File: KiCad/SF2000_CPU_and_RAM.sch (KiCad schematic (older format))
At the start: 5 parts, among them U10 IS61WV20488FBLL-10TLI, U11 IS61WV20488FBLL-10TLI, U12 IS61WV20488FBLL-10TLI, U8 68000D, U9 IS61WV20488FBLL-10TLI

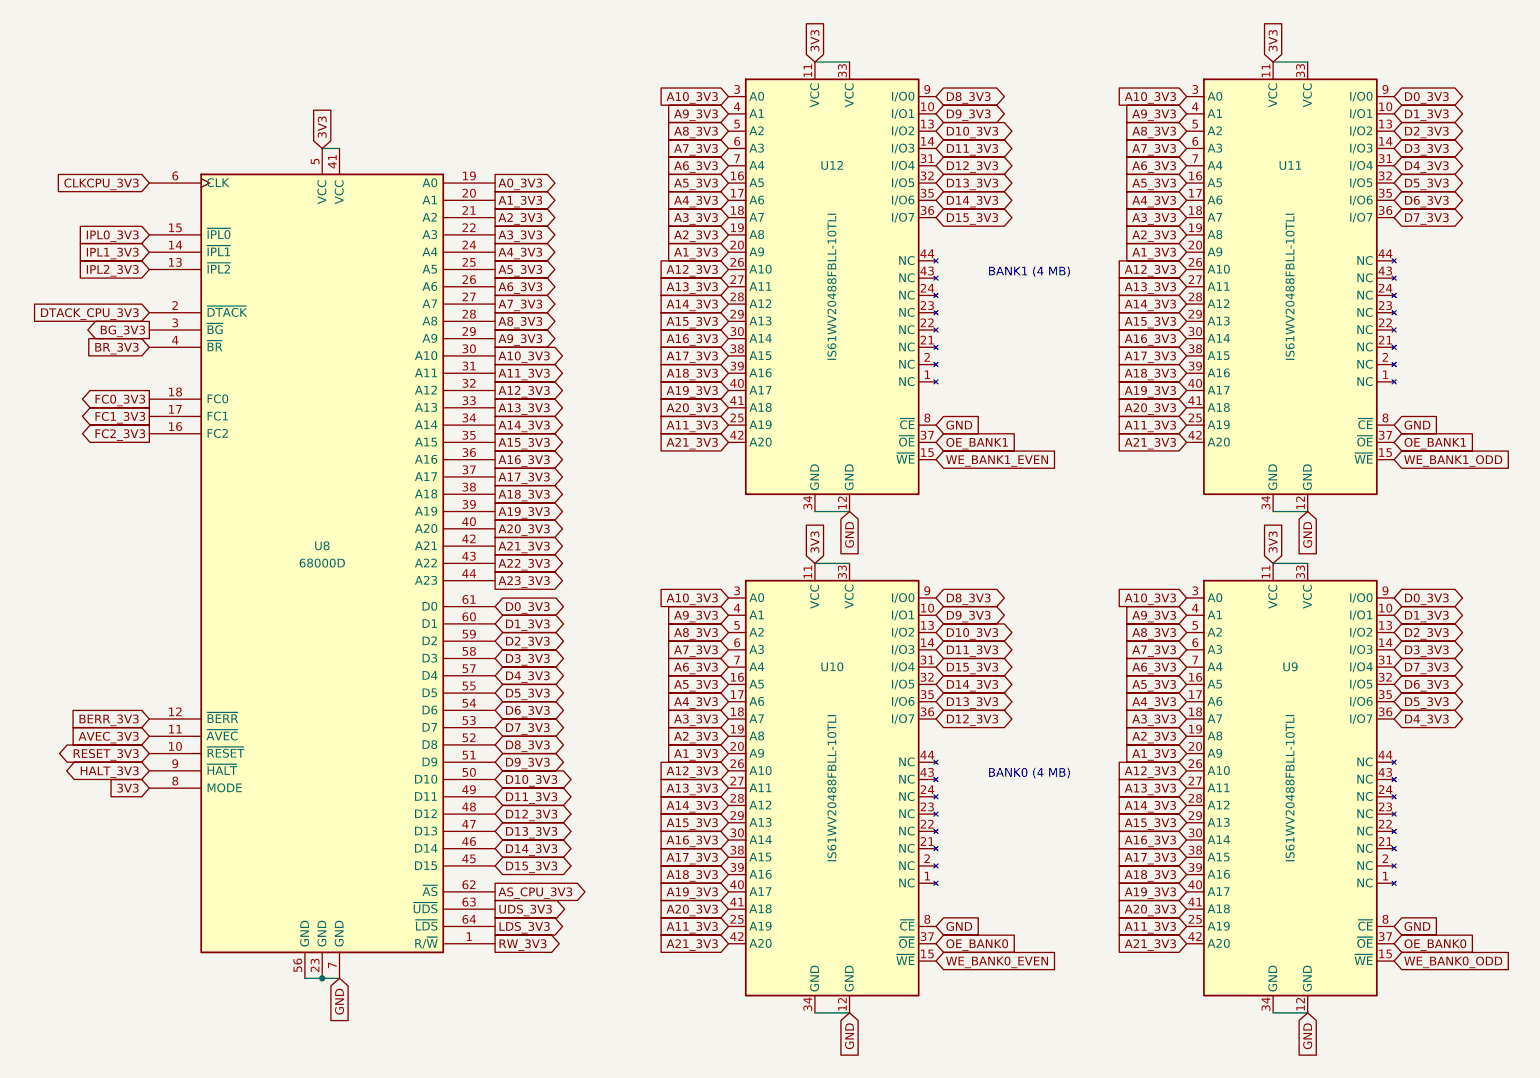
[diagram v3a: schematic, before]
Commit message: reconnected SRAMs and rerouted, and added a lot of caps
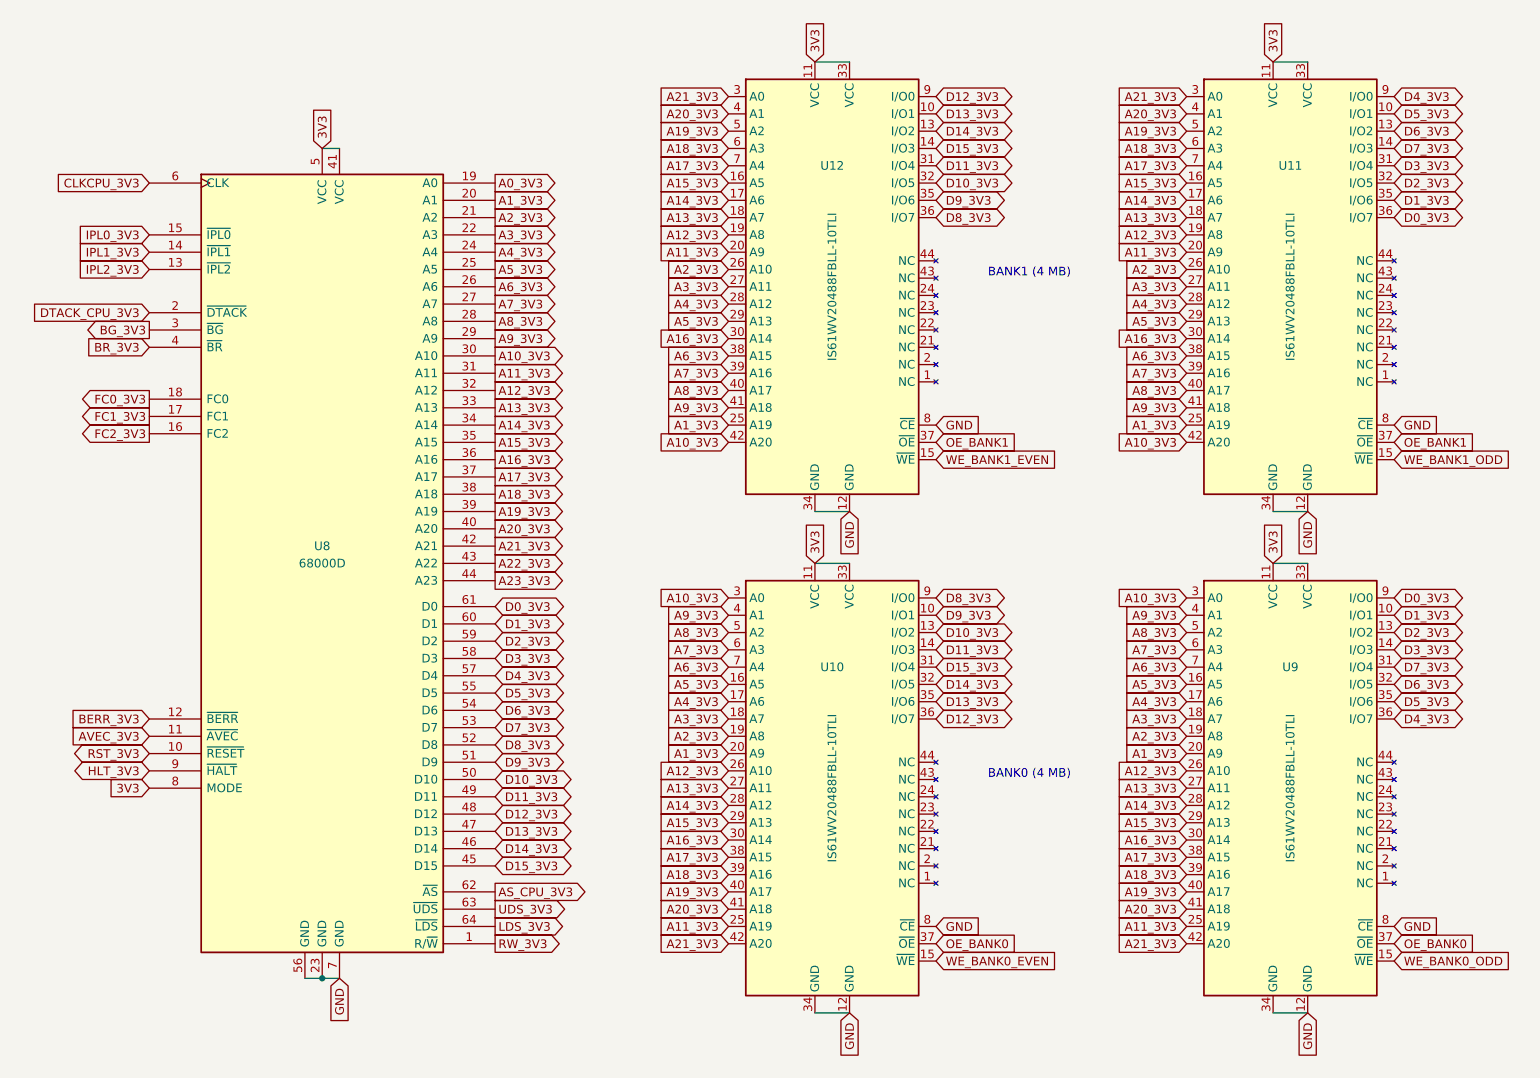
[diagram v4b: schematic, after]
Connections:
- net A10_3V3: now also U11.42 (A20), U12.42 (A20); no longer U11.3 (A0), U12.3 (A0)
- net A11_3V3: now also U11.20 (A9), U12.20 (A9); no longer U11.25 (A19), U12.25 (A19)
- net A12_3V3: now also U11.19 (A8), U12.19 (A8); no longer U11.26 (A10), U12.26 (A10)
- net A13_3V3: now also U11.18 (A7), U12.18 (A7); no longer U11.27 (A11), U12.27 (A11)
- net A14_3V3: now also U11.17 (A6), U12.17 (A6); no longer U11.28 (A12), U12.28 (A12)
- net A15_3V3: now also U11.16 (A5), U12.16 (A5); no longer U11.29 (A13), U12.29 (A13)
- net A17_3V3: now also U11.7 (A4), U12.7 (A4); no longer U11.38 (A15), U12.38 (A15)
- net A18_3V3: now also U11.6 (A3), U12.6 (A3); no longer U11.39 (A16), U12.39 (A16)
- net A19_3V3: now also U11.5 (A2), U12.5 (A2); no longer U11.40 (A17), U12.40 (A17)
- net A1_3V3: now also U11.25 (A19), U12.25 (A19); no longer U11.20 (A9), U12.20 (A9)
- net A20_3V3: now also U11.4 (A1), U12.4 (A1); no longer U11.41 (A18), U12.41 (A18)
- net A21_3V3: now also U11.3 (A0), U12.3 (A0); no longer U11.42 (A20), U12.42 (A20)
- net A2_3V3: now also U11.26 (A10), U12.26 (A10); no longer U11.19 (A8), U12.19 (A8)
- net A3_3V3: now also U11.27 (A11), U12.27 (A11); no longer U11.18 (A7), U12.18 (A7)
- net A4_3V3: now also U11.28 (A12), U12.28 (A12); no longer U11.17 (A6), U12.17 (A6)
- net A5_3V3: now also U11.29 (A13), U12.29 (A13); no longer U11.16 (A5), U12.16 (A5)
- net A6_3V3: now also U11.38 (A15), U12.38 (A15); no longer U11.7 (A4), U12.7 (A4)
- net A7_3V3: now also U11.39 (A16), U12.39 (A16); no longer U11.6 (A3), U12.6 (A3)
- net A8_3V3: now also U11.40 (A17), U12.40 (A17); no longer U11.5 (A2), U12.5 (A2)
- net A9_3V3: now also U11.41 (A18), U12.41 (A18); no longer U11.4 (A1), U12.4 (A1)
- net D0_3V3: now also U11.36 (I/O7); no longer U11.9 (I/O0)
- net D10_3V3: now also U12.32 (I/O5); no longer U12.13 (I/O2)
- net D11_3V3: now also U12.31 (I/O4); no longer U12.14 (I/O3)
- net D12_3V3: now also U12.9 (I/O0); no longer U12.31 (I/O4)
- net D13_3V3: now also U12.10 (I/O1); no longer U12.32 (I/O5)
- net D14_3V3: now also U12.13 (I/O2); no longer U12.35 (I/O6)
- net D15_3V3: now also U12.14 (I/O3); no longer U12.36 (I/O7)
- net D1_3V3: now also U11.35 (I/O6); no longer U11.10 (I/O1)
- net D2_3V3: now also U11.32 (I/O5); no longer U11.13 (I/O2)
- net D3_3V3: now also U11.31 (I/O4); no longer U11.14 (I/O3)
- net D4_3V3: now also U11.9 (I/O0); no longer U11.31 (I/O4)
- net D5_3V3: now also U11.10 (I/O1); no longer U11.32 (I/O5)
- net D6_3V3: now also U11.13 (I/O2); no longer U11.35 (I/O6)
- net D7_3V3: now also U11.14 (I/O3); no longer U11.36 (I/O7)
- net D8_3V3: now also U12.36 (I/O7); no longer U12.9 (I/O0)
- net D9_3V3: now also U12.35 (I/O6); no longer U12.10 (I/O1)
- net HALT_3V3 renamed HLT_3V3
- net RESET_3V3 renamed RST_3V3
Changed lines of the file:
@@
 AVEC_3V3
 Text GLabel 1500 4800 0    50   BiDi ~ 0
-RESET_3V3
+RST_3V3
 Text GLabel 1500 4900 0    50   BiDi ~ 0
-HALT_3V3
+HLT_3V3
 Text GLabel 1500 2450 0    50   Input ~ 0
 BR_3V3
@@
 Wire Wire Line
 	5350 6300 5550 6300
+Text GLabel 8700 1700 2    50   BiDi ~ 0
+D0_3V3
+Text GLabel 8700 1600 2    50   BiDi ~ 0
+D1_3V3
+Text GLabel 8700 1500 2    50   BiDi ~ 0
+D2_3V3
+Text GLabel 8700 1400 2    50   BiDi ~ 0
+D3_3V3
 Text GLabel 8700 1000 2    50   BiDi ~ 0
-D0_3V3
+D4_3V3
 Text GLabel 8700 1100 2    50   BiDi ~ 0
-D1_3V3
+D5_3V3
 Text GLabel 8700 1200 2    50   BiDi ~ 0
-D2_3V3
+D6_3V3
 Text GLabel 8700 1300 2    50   BiDi ~ 0
-D3_3V3
-Text GLabel 8700 1400 2    50   BiDi ~ 0
-D4_3V3
-Text GLabel 8700 1500 2    50   BiDi ~ 0
-D5_3V3
-Text GLabel 8700 1600 2    50   BiDi ~ 0
-D6_3V3
-Text GLabel 8700 1700 2    50   BiDi ~ 0
 D7_3V3
 Text GLabel 8700 3900 2    50   BiDi ~ 0
@@
 Text GLabel 6050 4300 2    50   BiDi ~ 0
 D15_3V3
+Text GLabel 6050 1700 2    50   BiDi ~ 0
+D8_3V3
+Text GLabel 6050 1600 2    50   BiDi ~ 0
+D9_3V3
+Text GLabel 6050 1500 2    50   BiDi ~ 0
+D10_3V3
+Text GLabel 6050 1400 2    50   BiDi ~ 0
+D11_3V3
 Text GLabel 6050 1000 2    50   BiDi ~ 0
-D8_3V3
+D12_3V3
 Text GLabel 6050 1100 2    50   BiDi ~ 0
-D9_3V3
+D13_3V3
 Text GLabel 6050 1200 2    50   BiDi ~ 0
-D10_3V3
+D14_3V3
 Text GLabel 6050 1300 2    50   BiDi ~ 0
-D11_3V3
-Text GLabel 6050 1400 2    50   BiDi ~ 0
-D12_3V3
-Text GLabel 6050 1500 2    50   BiDi ~ 0
-D13_3V3
-Text GLabel 6050 1600 2    50   BiDi ~ 0
-D14_3V3
-Text GLabel 6050 1700 2    50   BiDi ~ 0
 D15_3V3
+Text GLabel 4850 2900 0    50   Input ~ 0
+A1_3V3
+Text GLabel 4850 2000 0    50   Input ~ 0
+A2_3V3
+Text GLabel 4850 2100 0    50   Input ~ 0
+A3_3V3
+Text GLabel 4850 2200 0    50   Input ~ 0
+A4_3V3
+Text GLabel 4850 2300 0    50   Input ~ 0
+A5_3V3
+Text GLabel 4850 2500 0    50   Input ~ 0
+A6_3V3
+Text GLabel 4850 2600 0    50   Input ~ 0
+A7_3V3
+Text GLabel 4850 2700 0    50   Input ~ 0
+A8_3V3
+Text GLabel 4850 2800 0    50   Input ~ 0
+A9_3V3
+Text GLabel 4850 3000 0    50   Input ~ 0
+A10_3V3
 Text GLabel 4850 1900 0    50   Input ~ 0
-A1_3V3
+A11_3V3
 Text GLabel 4850 1800 0    50   Input ~ 0
-A2_3V3
+A12_3V3
 Text GLabel 4850 1700 0    50   Input ~ 0
-A3_3V3
+A13_3V3
 Text GLabel 4850 1600 0    50   Input ~ 0
-A4_3V3
+A14_3V3
 Text GLabel 4850 1500 0    50   Input ~ 0
-A5_3V3
-Text GLabel 4850 1400 0    50   Input ~ 0
-A6_3V3
-Text GLabel 4850 1300 0    50   Input ~ 0
-A7_3V3
-Text GLabel 4850 1200 0    50   Input ~ 0
-A8_3V3
-Text GLabel 4850 1100 0    50   Input ~ 0
-A9_3V3
-Text GLabel 4850 1000 0    50   Input ~ 0
-A10_3V3
-Text GLabel 4850 2900 0    50   Input ~ 0
-A11_3V3
-Text GLabel 4850 2000 0    50   Input ~ 0
-A12_3V3
-Text GLabel 4850 2100 0    50   Input ~ 0
-A13_3V3
-Text GLabel 4850 2200 0    50   Input ~ 0
-A14_3V3
-Text GLabel 4850 2300 0    50   Input ~ 0
 A15_3V3
 Text GLabel 4850 2400 0    50   Input ~ 0
 A16_3V3
-Text GLabel 4850 2500 0    50   Input ~ 0
+Text GLabel 4850 1400 0    50   Input ~ 0
 A17_3V3
-Text GLabel 4850 2600 0    50   Input ~ 0
+Text GLabel 4850 1300 0    50   Input ~ 0
 A18_3V3
-Text GLabel 4850 2700 0    50   Input ~ 0
+Text GLabel 4850 1200 0    50   Input ~ 0
 A19_3V3
-Text GLabel 4850 2800 0    50   Input ~ 0
+Text GLabel 4850 1100 0    50   Input ~ 0
 A20_3V3
-Text GLabel 4850 3000 0    50   Input ~ 0
+Text GLabel 4850 1000 0    50   Input ~ 0
 A21_3V3
-Text GLabel 7500 1900 0    50   Input ~ 0
-A1_3V3
-Text GLabel 7500 1800 0    50   Input ~ 0
-A2_3V3
-Text GLabel 7500 1700 0    50   Input ~ 0
-A3_3V3
-Text GLabel 7500 1600 0    50   Input ~ 0
-A4_3V3
-Text GLabel 7500 1500 0    50   Input ~ 0
-A5_3V3
-Text GLabel 7500 1400 0    50   Input ~ 0
-A6_3V3
-Text GLabel 7500 1300 0    50   Input ~ 0
-A7_3V3
-Text GLabel 7500 1200 0    50   Input ~ 0
-A8_3V3
-Text GLabel 7500 1100 0    50   Input ~ 0
-A9_3V3
-Text GLabel 7500 1000 0    50   Input ~ 0
-A10_3V3
 Text GLabel 4850 4800 0    50   Input ~ 0
 A1_3V3
@@
 Text GLabel 7500 3900 0    50   Input ~ 0
 A10_3V3
-Text GLabel 7500 2900 0    50   Input ~ 0
-A11_3V3
-Text GLabel 7500 2000 0    50   Input ~ 0
-A12_3V3
-Text GLabel 7500 2100 0    50   Input ~ 0
-A13_3V3
-Text GLabel 7500 2200 0    50   Input ~ 0
-A14_3V3
-Text GLabel 7500 2300 0    50   Input ~ 0
-A15_3V3
-Text GLabel 7500 2400 0    50   Input ~ 0
-A16_3V3
-Text GLabel 7500 2500 0    50   Input ~ 0
-A17_3V3
-Text GLabel 7500 2600 0    50   Input ~ 0
-A18_3V3
-Text GLabel 7500 2700 0    50   Input ~ 0
-A19_3V3
-Text GLabel 7500 2800 0    50   Input ~ 0
-A20_3V3
-Text GLabel 7500 3000 0    50   Input ~ 0
-A21_3V3
 Text GLabel 7500 5800 0    50   Input ~ 0
 A11_3V3
@@
 Text GLabel 4850 5900 0    50   Input ~ 0
 A21_3V3
+Text GLabel 7500 2900 0    50   Input ~ 0
+A1_3V3
+Text GLabel 7500 2000 0    50   Input ~ 0
+A2_3V3
+Text GLabel 7500 2100 0    50   Input ~ 0
+A3_3V3
+Text GLabel 7500 2200 0    50   Input ~ 0
+A4_3V3
+Text GLabel 7500 2300 0    50   Input ~ 0
+A5_3V3
+Text GLabel 7500 2500 0    50   Input ~ 0
+A6_3V3
+Text GLabel 7500 2600 0    50   Input ~ 0
+A7_3V3
+Text GLabel 7500 2700 0    50   Input ~ 0
+A8_3V3
+Text GLabel 7500 2800 0    50   Input ~ 0
+A9_3V3
+Text GLabel 7500 3000 0    50   Input ~ 0
+A10_3V3
+Text GLabel 7500 1900 0    50   Input ~ 0
+A11_3V3
+Text GLabel 7500 1800 0    50   Input ~ 0
+A12_3V3
+Text GLabel 7500 1700 0    50   Input ~ 0
+A13_3V3
+Text GLabel 7500 1600 0    50   Input ~ 0
+A14_3V3
+Text GLabel 7500 1500 0    50   Input ~ 0
+A15_3V3
+Text GLabel 7500 2400 0    50   Input ~ 0
+A16_3V3
+Text GLabel 7500 1400 0    50   Input ~ 0
+A17_3V3
+Text GLabel 7500 1300 0    50   Input ~ 0
+A18_3V3
+Text GLabel 7500 1200 0    50   Input ~ 0
+A19_3V3
+Text GLabel 7500 1100 0    50   Input ~ 0
+A20_3V3
+Text GLabel 7500 1000 0    50   Input ~ 0
+A21_3V3
 $EndSCHEMATC

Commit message: added IDE Activity LED-header and a header for IDE-pin 39 /Active
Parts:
- renumbered U9 to U10, U10 to U11, U11 to U12, U12 to U13, U8 to U9
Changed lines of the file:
@@
 $EndDescr
 $Comp
-L SF2000:68SEC000 U8
+L SF2000:68SEC000 U9
 U 1 1 621E09D7
 P 2500 3700
-F 0 "U8" H 2500 3800 50  0000 C CNN
+F 0 "U9" H 2500 3800 50  0000 C CNN
 F 1 "68000D" H 2500 3700 50  0000 C CNN
 F 2 "Package_QFP:LQFP-64_14x14mm_P0.8mm" H 2500 3700 50  0001 C CNN
@@
 3V3
 $Comp
-L SF2000:IS61WV20488FBLL-10TLI U12
+L SF2000:IS61WV20488FBLL-10TLI U13
 U 1 1 61F186AC
 P 5450 2100
-F 0 "U12" H 5450 2800 50  0000 C CNN
+F 0 "U13" H 5450 2800 50  0000 C CNN
 F 1 "IS61WV20488FBLL-10TLI" V 5450 2100 50  0000 C CNN
 F 2 "Package_SO:TSOP-II-44_10.16x18.41mm_P0.8mm" H 4950 3250 50  0001 C CNN
@@
 $EndComp
 $Comp
-L SF2000:IS61WV20488FBLL-10TLI U11
+L SF2000:IS61WV20488FBLL-10TLI U12
 U 1 1 61F2712B
 P 8100 2100
-F 0 "U11" H 8100 2800 50  0000 C CNN
+F 0 "U12" H 8100 2800 50  0000 C CNN
 F 1 "IS61WV20488FBLL-10TLI" V 8100 2100 50  0000 C CNN
 F 2 "Package_SO:TSOP-II-44_10.16x18.41mm_P0.8mm" H 7600 3250 50  0001 C CNN
@@
 $EndComp
 $Comp
-L SF2000:IS61WV20488FBLL-10TLI U10
+L SF2000:IS61WV20488FBLL-10TLI U11
 U 1 1 61F2A268
 P 5450 5000
-F 0 "U10" H 5450 5700 50  0000 C CNN
+F 0 "U11" H 5450 5700 50  0000 C CNN
 F 1 "IS61WV20488FBLL-10TLI" V 5450 5000 50  0000 C CNN
 F 2 "Package_SO:TSOP-II-44_10.16x18.41mm_P0.8mm" H 4950 6150 50  0001 C CNN
@@
 $EndComp
 $Comp
-L SF2000:IS61WV20488FBLL-10TLI U9
+L SF2000:IS61WV20488FBLL-10TLI U10
 U 1 1 61F2A272
 P 8100 5000
-F 0 "U9" H 8100 5700 50  0000 C CNN
+F 0 "U10" H 8100 5700 50  0000 C CNN
 F 1 "IS61WV20488FBLL-10TLI" V 8100 5000 50  0000 C CNN
 F 2 "Package_SO:TSOP-II-44_10.16x18.41mm_P0.8mm" H 7600 6150 50  0001 C CNN

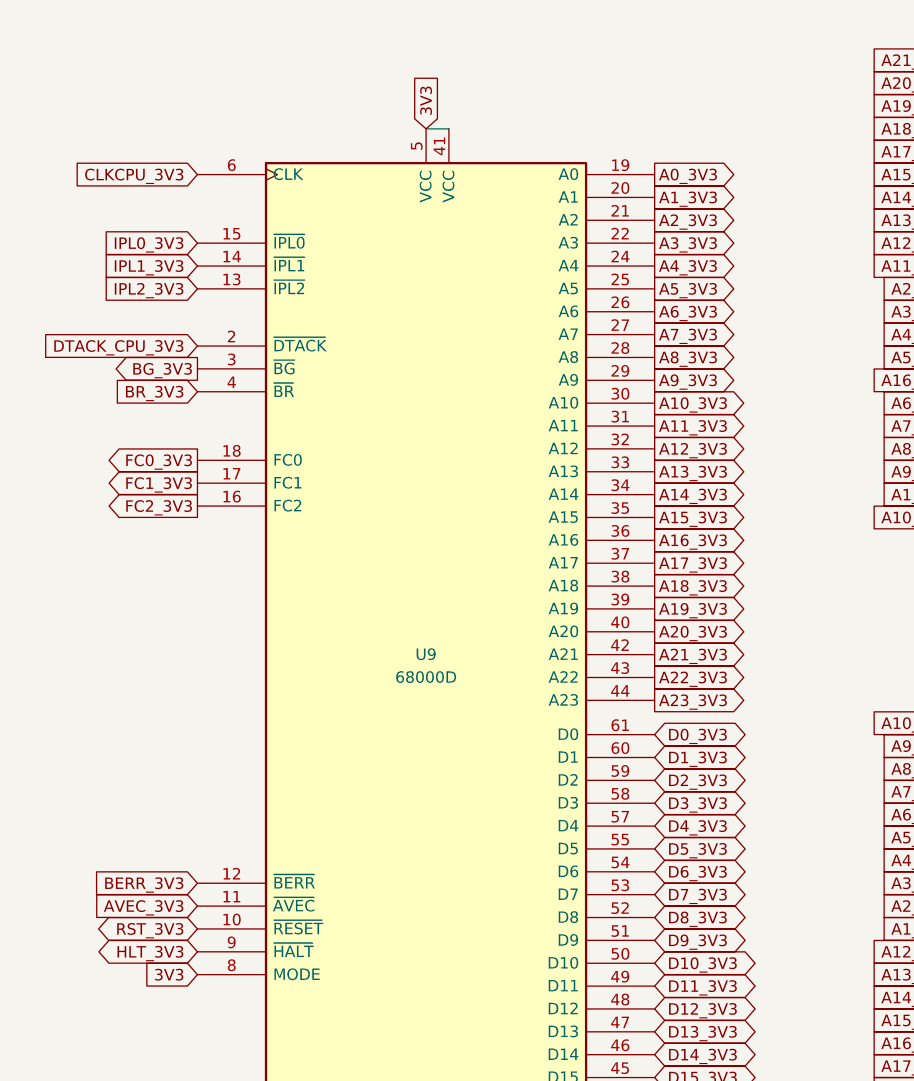
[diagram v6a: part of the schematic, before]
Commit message: removed CDAC-signal (not needed) and assigned E-signal to pin 11 (GCLKT_7) instead
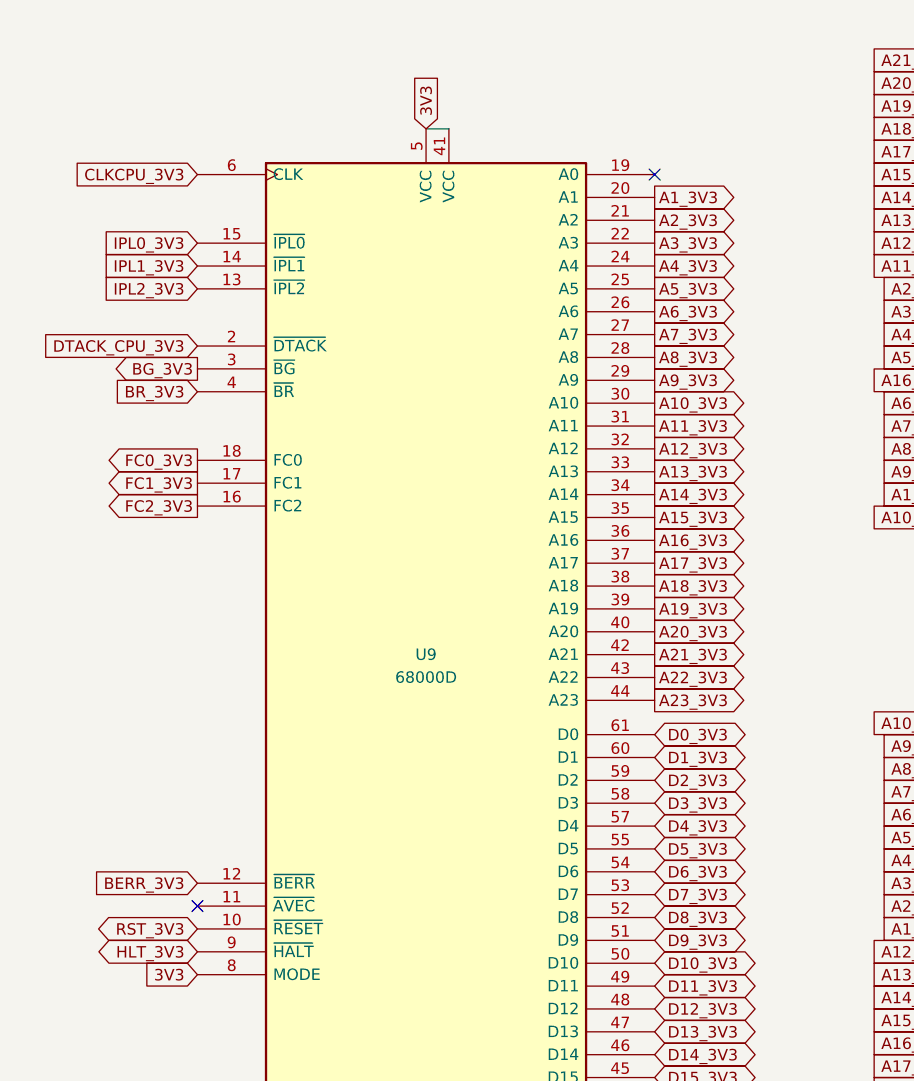
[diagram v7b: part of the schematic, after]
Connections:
- net A0_3V3: no longer names the net of U9.19 (A0)
- net AVEC_3V3: no longer names the net of U9.11 (~AVEC)
- no-connect marks 0 -> 2
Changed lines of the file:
@@
 Text GLabel 1500 2350 0    50   Output ~ 0
 BG_3V3
-Text GLabel 3500 1500 2    50   Output ~ 0
-A0_3V3
 Text GLabel 3500 3950 2    50   BiDi ~ 0
 D0_3V3
@@
 Wire Wire Line
 	2500 1300 2600 1300
-Text GLabel 1500 4700 0    50   Input ~ 0
-AVEC_3V3
 Text GLabel 1500 4800 0    50   BiDi ~ 0
 RST_3V3
@@
 Text GLabel 7500 1000 0    50   Input ~ 0
 A21_3V3
+NoConn ~ 1500 4700
+NoConn ~ 3500 1500
 $EndSCHEMATC
